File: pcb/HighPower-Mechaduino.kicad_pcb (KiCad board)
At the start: 2 copper layers, 60 x 60 mm, 121 parts, among them J1 SUPPLY, J2 STEPPER, P1 SWD, P2 USB, P3 PoStep25-32, P4 -, P5 -, P6 -, P7 -, Q1 SSM3J328R, Q10 IPD220N06L3, Q11 BSS138, Q2 BSS138, Q3 IPD220N06L3, Q4 IPD220N06L3, Q5 IPD220N06L3, Q6 IPD220N06L3, Q7 IPD220N06L3, Q8 IPD220N06L3, Q9 IPD220N06L3, SW1 SW_PUSH, U1 AS5047D, U2 AP2112K-3.3TRG1, U3 AT24CS64-SSHM, U4 SAMD21G18A-A, U5 A4955GLPTR-T, U6 A4955GLPTR-T, U7 USBLC6-2SC6, U8 MCP16331T, Y1 32.768kHz

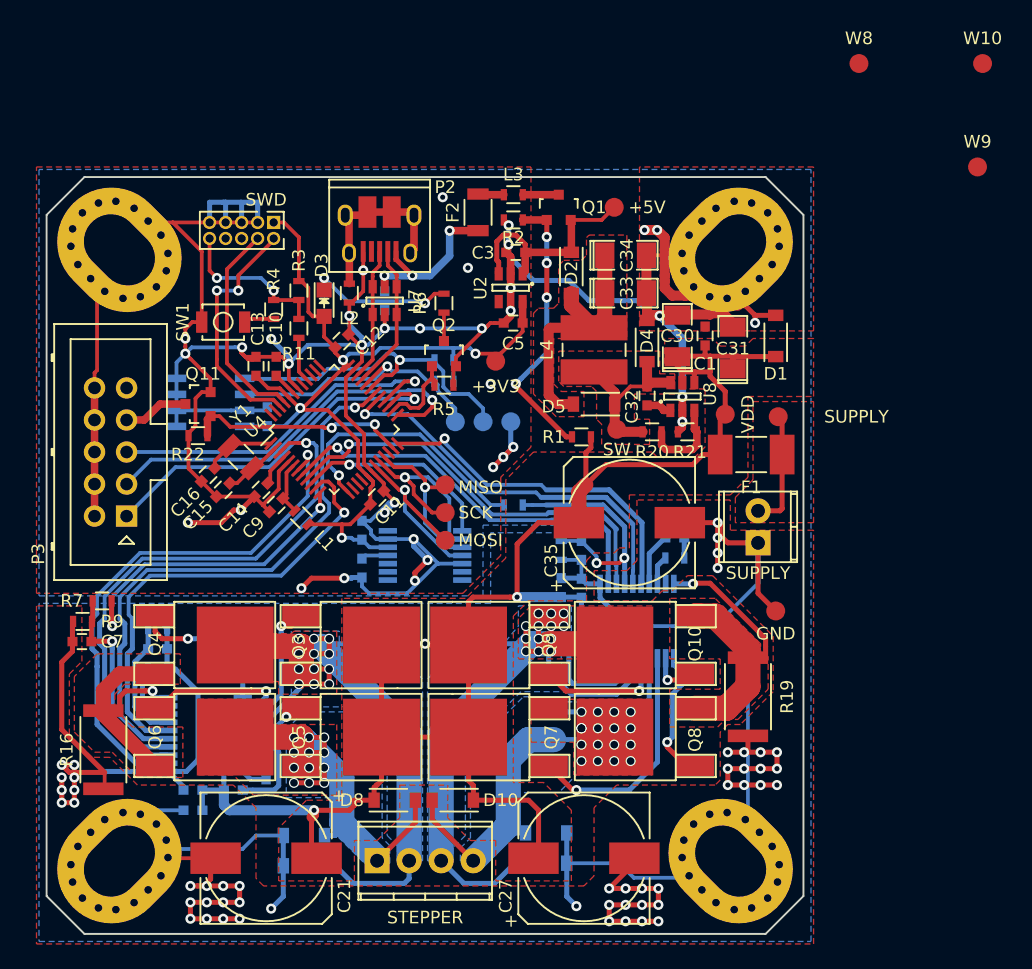
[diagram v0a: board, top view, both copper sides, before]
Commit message: Move processor part a bit down
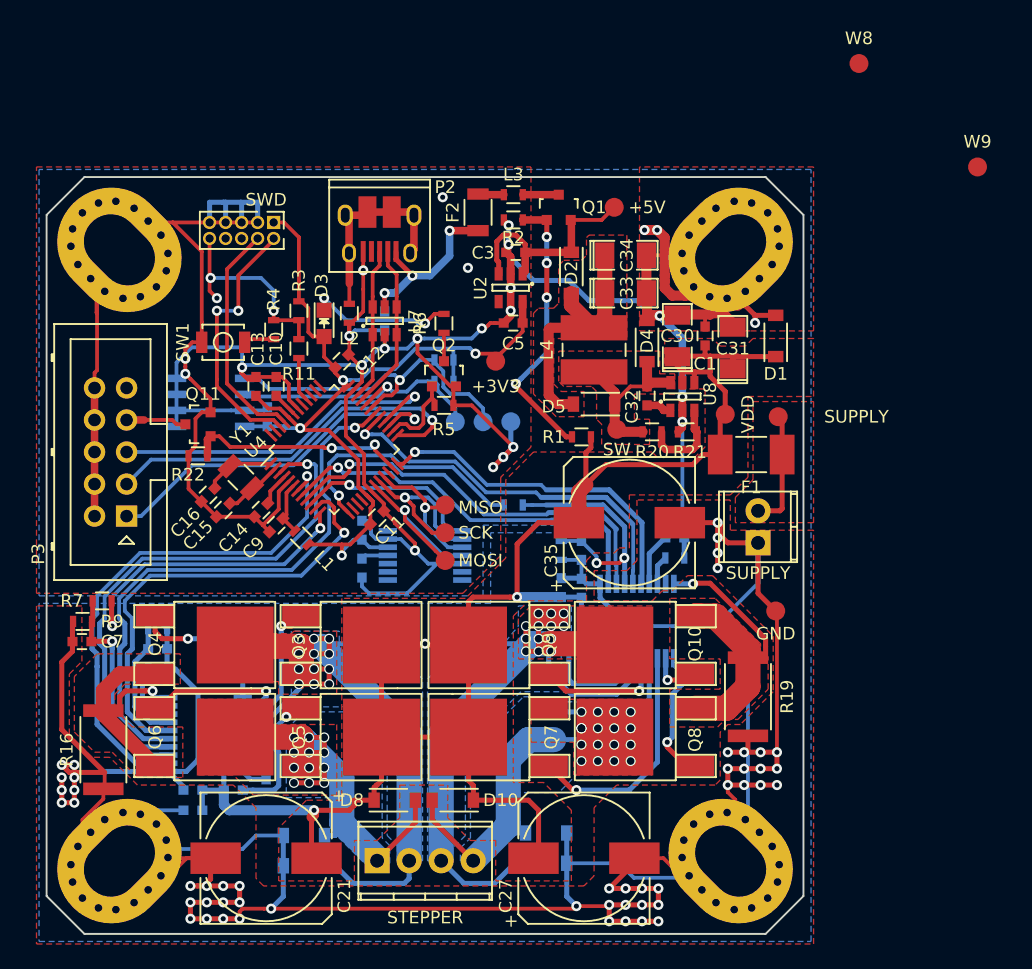
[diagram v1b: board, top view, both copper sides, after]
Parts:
- removed W10: AREF, Measurement_Points:Measurement_Point_Round-SMD-Pad_Small
- moved C14 1.60 mm to (137.0, 96.4)
- moved C15 1.60 mm to (134.0, 96.4)
- moved C16 1.60 mm to (132.8, 95.2)
- moved C29 1.60 mm to (146.8, 81.4)
- moved U7 1.60 mm to (146.8, 81.4)
- moved W16 1.60 mm to (151.6, 100.4)
- moved W17 1.60 mm to (151.6, 98.2)
- moved C10 1.60 mm to (138.2, 86.6)
- moved C11 1.60 mm to (146.2, 97.0)
- moved C12 1.60 mm to (143.4, 84.6)
- moved C13 1.60 mm to (136.6, 86.6)
- moved C9 1.60 mm to (138.2, 97.6)
- moved D3 1.60 mm to (142.0, 81.6)
- moved L1 1.60 mm to (140.2, 98.6)
- moved L2 1.60 mm to (144.0, 80.8)
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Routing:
- net GND: track 501.5 -> 586.3 mm, vias 83 -> 73
- net /RESET: track 12.5 -> 16.3 mm, vias 2 -> 3
- net +3V3: track 73.6 -> 75.8 mm
- net /USB_D-: track 11.6 -> 13.2 mm
- net /SWDIO: track 19.3 -> 20.9 mm
- net Net-(L2-Pad1): track 14.3 -> 15.9 mm
- net /USB_D+: track 10.5 -> 12.1 mm
- net /SWCLK: track 16.7 -> 18.3 mm
- net /SPI_SCK: track 15.7 -> 14.1 mm
- net /SPI_MISO: track 13.0 -> 11.5 mm
- net /SPI_MOSI: track 16.1 -> 14.8 mm
- net Net-(C29-Pad2): track 14.7 -> 15.8 mm
- net /SPI_CS0: track 16.2 -> 15.1 mm
- net /AIOUT1: track 42.3 -> 41.4 mm
- net /OCLn1: track 43.9 -> 43.1 mm
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
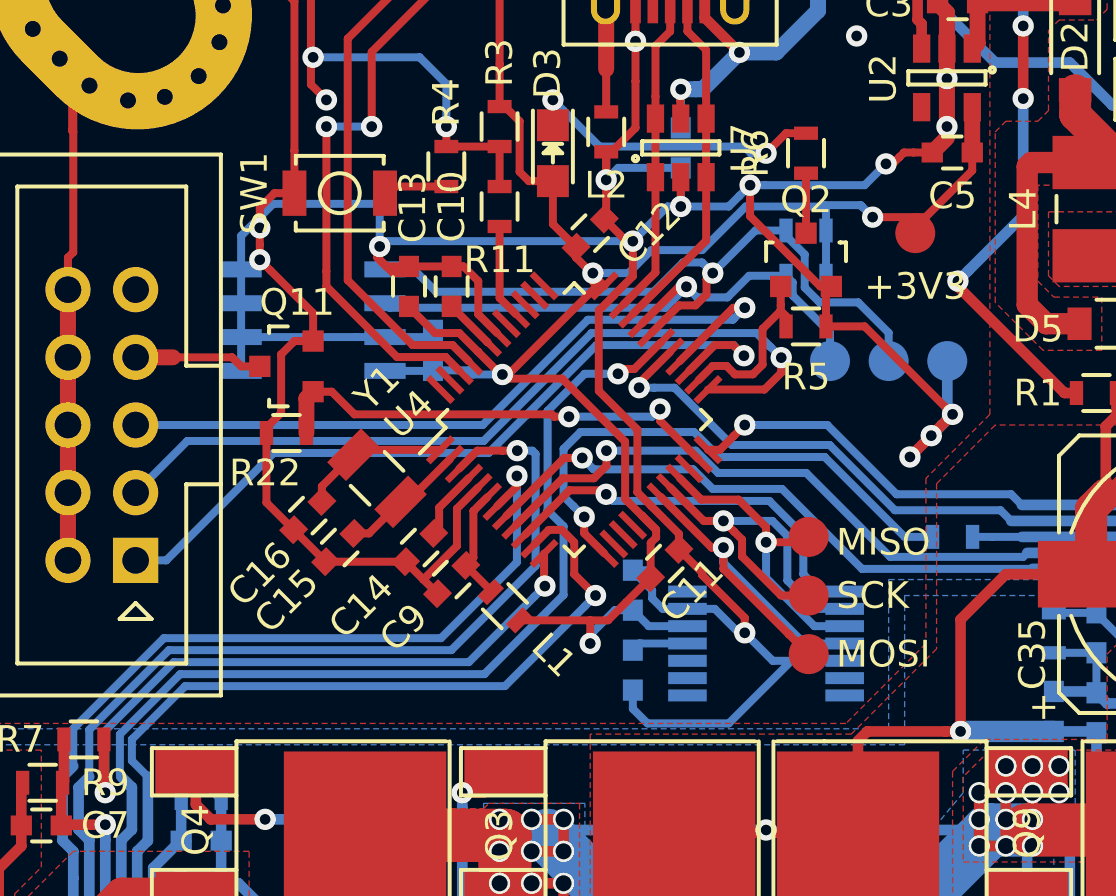
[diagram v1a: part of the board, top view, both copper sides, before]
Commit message: Add some little changes to the schematic, add calculations
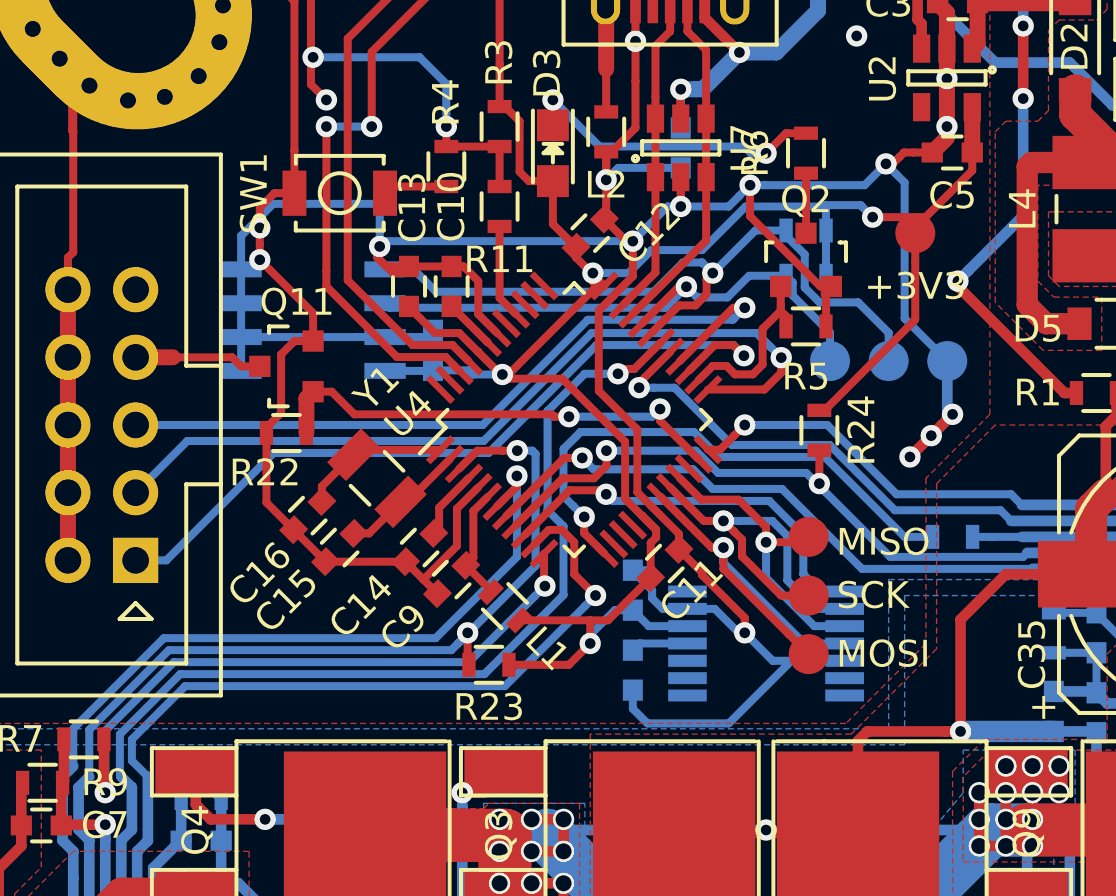
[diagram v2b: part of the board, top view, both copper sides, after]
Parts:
- added R23: 4k7, Resistors_SMD:R_0603, F.Cu at (139.6, 100.8)
- added R24: 4k7, Resistors_SMD:R_0603, F.Cu at (152.0, 92.0)
- C22, C28: value C -> 2.2n
- R14, R17: value R -> 22k
- R15, R18: value 20k -> 22k
- R20, R22, R3, R5: value 100k -> 22k
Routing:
- net +3V3: track 75.8 -> 87.4 mm
- net GND: track 586.3 -> 588.5 mm
- net /OCLn1: track 43.1 -> 44.9 mm, vias 1 -> 2
- net /OCLn2: track 32.7 -> 34.3 mm, vias 1 -> 2

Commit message: Use new library symbols
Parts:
- L1: value INDUCTOR_Small -> Ferrite_Bead
- L2, L3: value FERRIT_BEAD -> Ferrite_Bead
- R1, R2: value 100k -> 22k
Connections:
- F1 pad 1: Net-(F1-Pad1) -> VDD
- F1 pad 2: VDD -> Net-(F1-Pad2)
- J1 pad 2: Net-(F1-Pad1) -> Net-(F1-Pad2)
- L3 pad 1: Net-(F2-Pad1) -> /Protected_USB_Supply/VBUS
- L3 pad 2: /Protected_USB_Supply/VBUS -> Net-(F2-Pad1)
- W1 pad 1: Net-(F1-Pad1) -> Net-(F1-Pad2)
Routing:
- net Net-(F1-Pad1): track 9.40 -> 0.00 mm
- net Net-(F1-Pad2): track 0.00 -> 9.05 mm
- net /Protected_USB_Supply/VBUS: track 2.85 -> 0.00 mm
- net Net-(F2-Pad1): track 2.07 -> 4.92 mm
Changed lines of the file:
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@@
   (general
     (links 276)
-    (no_connects 3)
+    (no_connects 8)
     (area 119.924999 69.924999 180.075001 130.075001)
     (thickness 1.6)
@@
     (zones 0)
     (modules 122)
-    (nets 99)
+    (nets 100)
   )
   (page A4)
@@
   (net 97 /PWM_Bridge_A4955-B/VREF)
   (net 98 "Net-(P3-Pad7)")
+  (net 99 "Net-(F1-Pad2)")
   (net_class Default "Dies ist die voreingestellte Netzklasse."
     (clearance 0.15)
@@
     (add_net "Net-(C9-Pad2)")
     (add_net "Net-(D3-Pad1)")
-    (add_net "Net-(F1-Pad1)")
+    (add_net "Net-(F1-Pad2)")
     (add_net "Net-(F2-Pad1)")
     (add_net "Net-(L2-Pad1)")
@@
     (fp_circle (center 0 0) (end 1 0) (layer F.CrtYd) (width 0.05))
     (pad 1 smd circle (at 0 0) (size 1.5 1.5) (layers F.Cu F.Mask)
-      (net 24 "Net-(F1-Pad1)") (zone_connect 2))
+      (net 99 "Net-(F1-Pad2)") (zone_connect 2))
   )
   (module Measurement_Points:Measurement_Point_Round-SMD-Pad_Small (layer F.Cu)
@@
     (fp_line (start -1.7 -3.3) (end 4.3 -3.3) (layer F.CrtYd) (width 0.05))
     (pad 2 thru_hole oval (at 2.54 0 90) (size 1.99898 1.99898) (drill 1.09728) (layers *.Cu *.Mask F.SilkS)
-      (net 24 "Net-(F1-Pad1)"))
+      (net 99 "Net-(F1-Pad2)"))
     (pad 1 thru_hole rect (at 0 0 90) (size 1.99898 1.99898) (drill 1.09728) (layers *.Cu *.Mask F.SilkS)
       (net 1 GND))
@@
       (effects (font (size 1 1) (thickness 0.15)))
     )
-    (fp_text value INDUCTOR_Small (at 0 1.9 135) (layer F.Fab)
+    (fp_text value Ferrite_Bead (at 0 1.9 135) (layer F.Fab)
       (effects (font (size 1 1) (thickness 0.15)))
     )
@@
       (effects (font (size 1 1) (thickness 0.15)))
     )
-    (fp_text value FERRIT_BEAD (at 0 1.9 270) (layer F.Fab)
+    (fp_text value Ferrite_Bead (at 0 1.9 270) (layer F.Fab)
       (effects (font (size 1 1) (thickness 0.15)))
     )
@@
       (effects (font (size 1 1) (thickness 0.15)))
     )
-    (fp_text value FERRIT_BEAD (at 0 1.9) (layer F.Fab)
+    (fp_text value Ferrite_Bead (at 0 1.9) (layer F.Fab)
       (effects (font (size 1 1) (thickness 0.15)))
     )
@@
     (fp_line (start -0.5 -0.675) (end 0.5 -0.675) (layer F.SilkS) (width 0.15))
     (pad 2 smd rect (at 0.75 0) (size 0.5 0.9) (layers F.Cu F.Paste F.Mask)
-      (net 30 /Protected_USB_Supply/VBUS))
-    (pad 1 smd rect (at -0.75 0) (size 0.5 0.9) (layers F.Cu F.Paste F.Mask)
       (net 25 "Net-(F2-Pad1)"))
+    (pad 1 smd rect (at -0.75 0) (size 0.5 0.9) (layers F.Cu F.Paste F.Mask)
+      (net 30 /Protected_USB_Supply/VBUS))
     (model Resistors_SMD.3dshapes/R_0603.wrl
       (at (xyz 0 0 0))
@@
       (effects (font (size 1 1) (thickness 0.15)))
     )
-    (fp_text value 100k (at -3.2 0) (layer F.Fab)
+    (fp_text value 22k (at -3.2 0) (layer F.Fab)
       (effects (font (size 1 1) (thickness 0.15)))
     )
@@
       (effects (font (size 1 1) (thickness 0.15)))
     )
-    (fp_text value 100k (at 0 1.9) (layer F.Fab)
+    (fp_text value 22k (at 0 1.9) (layer F.Fab)
       (effects (font (size 1 1) (thickness 0.15)))
     )
@@
     (fp_line (start -3.05 -1.27) (end 3.05 -1.27) (layer F.Fab) (width 0.1))
     (pad 2 smd rect (at 2.455 0 180) (size 1.96 3.15) (layers F.Cu F.Paste F.Mask)
-      (net 2 VDD))
+      (net 99 "Net-(F1-Pad2)"))
     (pad 1 smd rect (at -2.455 0 180) (size 1.96 3.15) (layers F.Cu F.Paste F.Mask)
-      (net 24 "Net-(F1-Pad1)"))
+      (net 2 VDD))
   )
   (module Mounting_Holes_local:MountingHole_4.3x6.2mm_M4_Pad_Via locked (layer F.Cu)
@@
   (segment (start 170.45 85.45) (end 170 85) (width 0.4) (layer F.Cu) (net 2))
   (segment (start 170 85) (end 170 84.251) (width 0.4) (layer F.Cu) (net 2))
-  (segment (start 171.22 92.8) (end 164.35 92.8) (width 0.4) (layer F.Cu) (net 2))
   (segment (start 164.35 92.8) (end 162.75 94.4) (width 0.4) (layer F.Cu) (net 2))
-  (segment (start 173.4 92) (end 172.02 92) (width 0.4) (layer F.Cu) (net 2))
-  (segment (start 172.02 92) (end 171.22 92.8) (width 0.4) (layer F.Cu) (net 2))
   (segment (start 153.45 114.4) (end 153.45 117.848) (width 0.4) (layer F.Cu) (net 2))
   (segment (start 153.45 117.848) (end 153.835 118.233) (width 0.4) (layer F.Cu) (net 2))
@@
   (segment (start 173.8 88.8) (end 173.8 87) (width 0.4) (layer F.Cu) (net 2))
   (segment (start 171.35 86.3) (end 171.35 85.45) (width 0.4) (layer F.Cu) (net 2))
-  (segment (start 173.4 92) (end 173.4 89.2) (width 0.4) (layer F.Cu) (net 2))
   (segment (start 173.4 89.2) (end 173.8 88.8) (width 0.4) (layer F.Cu) (net 2))
   (segment (start 162.2 97.4) (end 159 97.4) (width 0.4) (layer F.Cu) (net 2))
@@
   (segment (start 159 123.6) (end 159 124) (width 0.4) (layer F.Cu) (net 2))
   (segment (start 159 124) (end 158.25 124) (width 2) (layer F.Cu) (net 2))
+  (segment (start 178.31 96.29) (end 178.31 92) (width 0.4) (layer F.Cu) (net 2))
+  (segment (start 171.22 92.8) (end 164.35 92.8) (width 0.4) (layer F.Cu) (net 2))
+  (segment (start 172.02 92) (end 171.22 92.8) (width 0.4) (layer F.Cu) (net 2))
+  (segment (start 178.14 96.46) (end 178.31 96.29) (width 0.4) (layer F.Cu) (net 2))
   (segment (start 140.35 100.8) (end 142.6 100.8) (width 0.3) (layer F.Cu) (net 3))
   (segment (start 142.6 100.8) (end 143.4 100) (width 0.3) (layer F.Cu) (net 3))
@@
   (via (at 142 79.6) (size 0.8) (drill 0.4) (layers F.Cu B.Cu) (net 23))
   (segment (start 142 80.55098) (end 142 79.65154) (width 0.3) (layer F.Cu) (net 23))
-  (segment (start 178.31 92) (end 178.31 89.31) (width 0.4) (layer F.Cu) (net 24))
-  (segment (start 178.31 89.31) (end 178 89) (width 0.4) (layer F.Cu) (net 24))
-  (segment (start 178.14 96.46) (end 178.31 96.29) (width 0.4) (layer F.Cu) (net 24))
-  (segment (start 178.31 96.29) (end 178.31 92) (width 0.4) (layer F.Cu) (net 24))
-  (segment (start 176.4 96.46) (end 178.14 96.46) (width 0.4) (layer F.Cu) (net 24))
   (segment (start 156.25 71.4) (end 154.25 71.4) (width 0.6) (layer F.Cu) (net 25))
   (segment (start 154.25 71.4) (end 154.2 71.35) (width 0.6) (layer F.Cu) (net 25))
+  (segment (start 157.75 71.4) (end 160.59822 71.4) (width 0.6) (layer F.Cu) (net 25))
   (segment (start 143.636399 88.800012) (end 148.769403 88.800012) (width 0.3) (layer B.Cu) (net 26))
   (segment (start 139.5864 92.850011) (end 143.636399 88.800012) (width 0.3) (layer B.Cu) (net 26))
@@
   (segment (start 144 78.45) (end 144 76.05) (width 0.6) (layer F.Cu) (net 29))
   (segment (start 144 76.05) (end 143.975 76.025) (width 0.6) (layer F.Cu) (net 29))
-  (segment (start 157.75 71.4) (end 160.59822 71.4) (width 0.6) (layer F.Cu) (net 30))
   (segment (start 160.59822 71.4) (end 160.6 71.40178) (width 0.6) (layer F.Cu) (net 30))
   (segment (start 138.840202 89.407969) (end 138.232233 88.8) (width 0.3) (layer F.Cu) (net 31))
@@
   (segment (start 130.30173 89.6) (end 129.96173 89.26) (width 0.3) (layer F.Cu) (net 98))
   (segment (start 126.34 89.26) (end 127.74 89.26) (width 0.6) (layer F.Cu) (net 98))
+  (segment (start 173.4 92) (end 172.02 92) (width 0.4) (layer F.Cu) (net 99))
+  (segment (start 173.4 92) (end 173.4 89.2) (width 0.4) (layer F.Cu) (net 99))
+  (segment (start 178.31 92) (end 178.31 89.31) (width 0.4) (layer F.Cu) (net 99))
+  (segment (start 178.31 89.31) (end 178 89) (width 0.4) (layer F.Cu) (net 99))
+  (segment (start 176.4 96.46) (end 178.14 96.46) (width 0.4) (layer F.Cu) (net 99))
   (zone (net 1) (net_name GND) (layer B.Cu) (hatch edge 0.508)
     (connect_pads (clearance 0.508))

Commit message: Improve pcb routing
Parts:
- added REF***: KiCad-Logo2_8mm_SilkScreen, Symbols:KiCad-Logo2_8mm_SilkScreen, B.Cu at (170.4, 87.6)
- added REF***: OSHW-Logo_11.4x12mm_SilkScreen, Symbols:OSHW-Logo_11.4x12mm_SilkScreen, B.Cu at (150.0, 115.4)
- U5, U6: footprint Housings_SSOP:TSSOP-20_4.4x6.5mm_Pitch0.65mm -> Housings_SSOP:ETSSOP-20-1EP_4.4x6.5mm_Pitch0.65mm
- W1: value SUPPLY -> SUPL
- moved W9 56.2 mm to (139.6, 84.0)
- moved W8 48.4 mm to (141.8, 84.0)
- moved D3 12.1 mm to (153.0, 76.6), turned to 0 degrees
- moved R11 6.51 mm to (135.6, 78.8)
- moved R4 5.19 mm to (134.0, 78.8)
- moved Q2 4.10 mm to (150.6, 81.6)
- moved R5 3.81 mm to (150.6, 84.4)
- moved L2 3.44 mm to (141.2, 78.8)
- moved R3 3.33 mm to (137.2, 78.8), turned to 270 degrees
- moved R6 2.82 mm to (151.2, 78.8), turned to 0 degrees
- moved R23 2.40 mm to (142.0, 100.8)
- moved SW1 1.08 mm to (133.4, 82.2)
- moved P1 1.02 mm to (138.2, 72.6)
- moved R24 1.00 mm to (152.6, 92.8), turned to 0 degrees
- moved C29 0.80 mm to (146.8, 80.6)
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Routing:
- net GND: track 588.5 -> 548.4 mm, vias 73 -> 78
- net +3V3: track 87.4 -> 99.9 mm
- net Net-(D3-Pad1): track 11.6 -> 2.20 mm, vias 2 -> 0
- net /RESET: track 16.3 -> 7.74 mm, vias 3 -> 0
- net /PWM_Bridge_A4955-B/OUT2: track 59.9 -> 51.7 mm
- net Net-(R11-Pad2): track 3.54 -> 10.2 mm
- net /LED_D13: track 6.79 -> 10.5 mm
- net /Arduino_Zero_Base/Arduino_RXD: track 0.00 -> 3.64 mm
- net /Arduino_Zero_Base/Arduino_TXD: track 0.00 -> 3.19 mm
- net /SWCLK: track 18.3 -> 20.4 mm, vias 0 -> 1
- net Net-(Q1-Pad1): track 22.3 -> 20.4 mm
- net (no net): track 0.00 -> 1.40 mm, vias 2 -> 0
- net /OCLn1: track 44.9 -> 46.1 mm
- net VDD: track 149.5 -> 150.7 mm
- net /IN1: track 36.9 -> 35.8 mm
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- added copper zone on F.Cu, net Net-(F1-Pad2)
- removed copper zone on F.Cu, net Net-(F1-Pad1)
